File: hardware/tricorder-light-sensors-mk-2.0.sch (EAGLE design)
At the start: 8 parts, among them U1 VEML6075, U2 APDS-9250

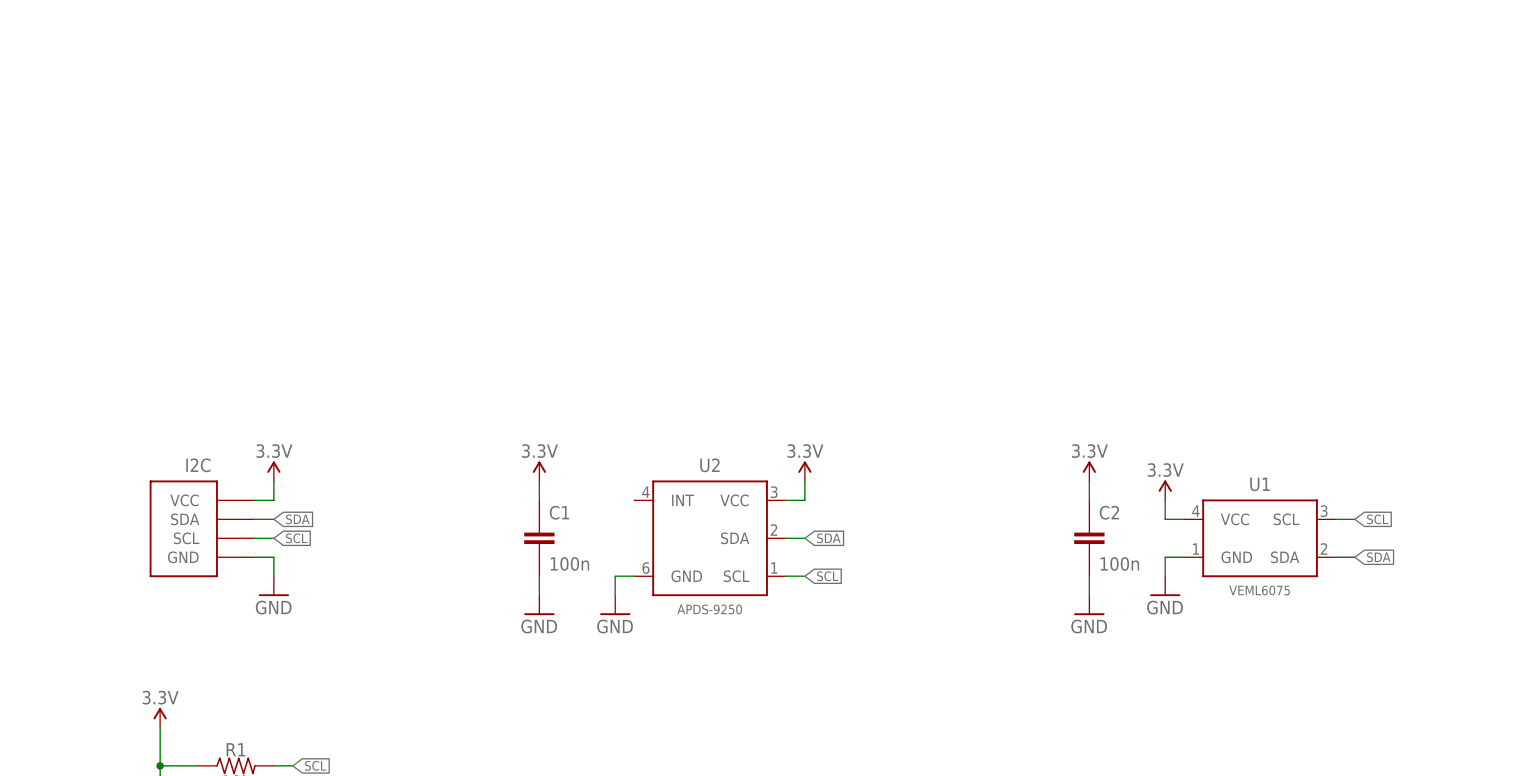
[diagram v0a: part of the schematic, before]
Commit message: swap apds9250 for tcs3400
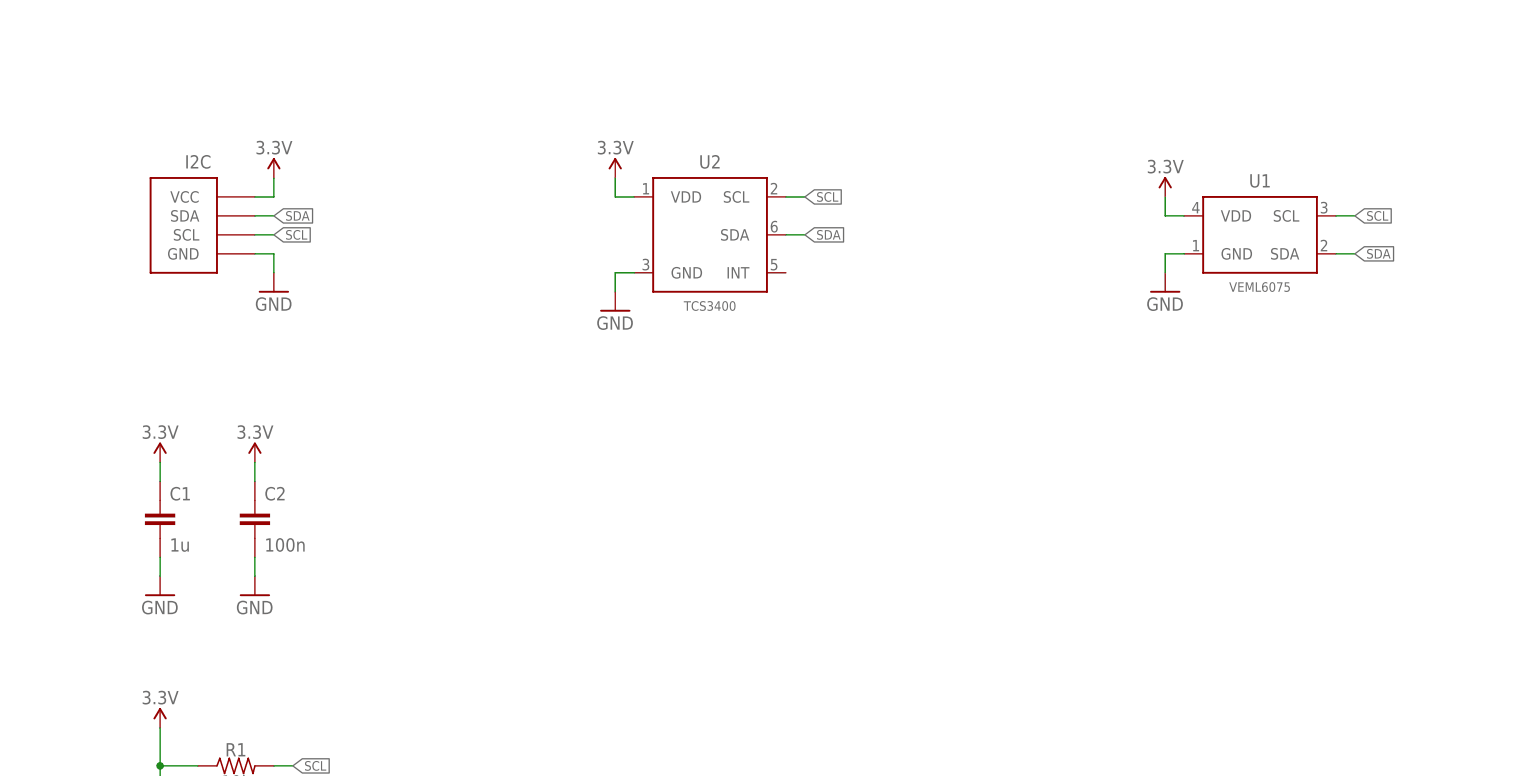
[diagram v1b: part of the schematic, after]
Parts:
- C1: value 100n -> 1u
- U2: value APDS-9250 -> TCS3400; device a_parts:APDS-9250ALT -> a_parts:TCS3400DFN6
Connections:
- net 3.3V: now also U1.VDD, U2.VDD; no longer U1.VCC, U2.VCC
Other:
- moved on the sheet: C1, C2, I2C, U1, U2
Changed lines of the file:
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@@
 </part>
 <part name="GND1" library="a_parts" deviceset="GND" device=""/>
-<part name="C1" library="a_parts" deviceset="CAPACITOR-CERAMIC" device="C0603" value="100n"/>
+<part name="C1" library="a_parts" deviceset="CAPACITOR-CERAMIC" device="C0603" value="1u"/>
 <part name="SUPPLY3" library="a_parts" deviceset="3.3V" device=""/>
 <part name="C2" library="a_parts" deviceset="CAPACITOR-CERAMIC" device="C0603" value="100n"/>
 <part name="SUPPLY4" library="a_parts" deviceset="3.3V" device=""/>
 <part name="GND4" library="a_parts" deviceset="GND" device=""/>
-<part name="U2" library="a_parts" deviceset="APDS-9250" device="ALT" value="APDS-9250"/>
 <part name="U1" library="a_parts" deviceset="VEML6075" device=""/>
 <part name="I2C" library="a_parts" deviceset="M04-I2C" device="PTH-0.1IN-CENTERED" value="M04-I2CPTH-0.1IN-CENTERED"/>
@@
 <part name="R1" library="a_parts" deviceset="RESISTOR" device="R0603" value="10k"/>
 <part name="R2" library="a_parts" deviceset="RESISTOR" device="R0603" value="10k"/>
+<part name="U2" library="a_parts" deviceset="TCS3400" device="DFN6" value="TCS3400"/>
 </parts>
 <sheets>
 <sheet>
 <plain>
-<text x="93.98" y="83.82" size="1.778" layer="90">RGB, IR, Ambient</text>
-<text x="172.72" y="83.82" size="1.778" layer="90">UVA, UVB</text>
+<text x="93.98" y="124.46" size="1.778" layer="90">RGB, IR, Ambient</text>
+<text x="172.72" y="124.46" size="1.778" layer="90">UVA, UVB</text>
 <wire x1="35.56" y1="185.42" x2="33.02" y2="185.42" width="0.1524" layer="90" style="shortdash"/>
 </plain>
@@
 <instance part="FRAME1" gate="G$1" x="0" y="0"/>
 <instance part="FRAME1" gate="V" x="152.4" y="0"/>
-<instance part="GND1" gate="1" x="81.28" y="91.44"/>
-<instance part="C1" gate="G$1" x="81.28" y="101.6"/>
-<instance part="SUPPLY3" gate="G$1" x="81.28" y="109.22"/>
-<instance part="C2" gate="G$1" x="154.94" y="101.6"/>
-<instance part="SUPPLY4" gate="G$1" x="154.94" y="109.22"/>
-<instance part="GND4" gate="1" x="154.94" y="91.44"/>
-<instance part="U2" gate="G$1" x="104.14" y="101.6"/>
-<instance part="U1" gate="G$1" x="177.8" y="101.6"/>
-<instance part="I2C" gate="G$1" x="35.56" y="104.14" rot="MR0"/>
-<instance part="SUPPLY1" gate="G$1" x="45.72" y="109.22"/>
-<instance part="GND2" gate="1" x="45.72" y="93.98"/>
-<instance part="SUPPLY2" gate="G$1" x="116.84" y="109.22"/>
-<instance part="SUPPLY5" gate="G$1" x="165.1" y="106.68"/>
-<instance part="GND7" gate="1" x="165.1" y="93.98"/>
-<instance part="GND8" gate="1" x="91.44" y="91.44"/>
+<instance part="GND1" gate="1" x="30.48" y="93.98"/>
+<instance part="C1" gate="G$1" x="30.48" y="104.14"/>
+<instance part="SUPPLY3" gate="G$1" x="30.48" y="111.76"/>
+<instance part="C2" gate="G$1" x="43.18" y="104.14"/>
+<instance part="SUPPLY4" gate="G$1" x="43.18" y="111.76"/>
+<instance part="GND4" gate="1" x="43.18" y="93.98"/>
+<instance part="U1" gate="G$1" x="177.8" y="142.24"/>
+<instance part="I2C" gate="G$1" x="35.56" y="144.78" rot="MR0"/>
+<instance part="SUPPLY1" gate="G$1" x="45.72" y="149.86"/>
+<instance part="GND2" gate="1" x="45.72" y="134.62"/>
+<instance part="SUPPLY2" gate="G$1" x="91.44" y="149.86"/>
+<instance part="SUPPLY5" gate="G$1" x="165.1" y="147.32"/>
+<instance part="GND7" gate="1" x="165.1" y="134.62"/>
+<instance part="GND8" gate="1" x="91.44" y="132.08"/>
 <instance part="SUPPLY8" gate="G$1" x="30.48" y="76.2"/>
 <instance part="R1" gate="G$1" x="40.64" y="71.12"/>
 <instance part="R2" gate="G$1" x="40.64" y="63.5"/>
+<instance part="U2" gate="G$1" x="104.14" y="142.24"/>
 </instances>
 <busses>
@@
 <pinref part="GND1" gate="1" pin="GND"/>
 <pinref part="C1" gate="G$1" pin="2"/>
-<wire x1="81.28" y1="96.52" x2="81.28" y2="93.98" width="0.1524" layer="91"/>
+<wire x1="30.48" y1="99.06" x2="30.48" y2="96.52" width="0.1524" layer="91"/>
 </segment>
 <segment>
 <pinref part="C2" gate="G$1" pin="2"/>
 <pinref part="GND4" gate="1" pin="GND"/>
-<wire x1="154.94" y1="93.98" x2="154.94" y2="96.52" width="0.1524" layer="91"/>
+<wire x1="43.18" y1="96.52" x2="43.18" y2="99.06" width="0.1524" layer="91"/>
 </segment>
 <segment>
 <pinref part="GND2" gate="1" pin="GND"/>
-<wire x1="45.72" y1="96.52" x2="45.72" y2="99.06" width="0.1524" layer="91"/>
+<wire x1="45.72" y1="137.16" x2="45.72" y2="139.7" width="0.1524" layer="91"/>
 <pinref part="I2C" gate="G$1" pin="GND"/>
-<wire x1="45.72" y1="99.06" x2="43.18" y2="99.06" width="0.1524" layer="91"/>
+<wire x1="45.72" y1="139.7" x2="43.18" y2="139.7" width="0.1524" layer="91"/>
 </segment>
 <segment>
 <pinref part="GND7" gate="1" pin="GND"/>
-<wire x1="165.1" y1="96.52" x2="165.1" y2="99.06" width="0.1524" layer="91"/>
+<wire x1="165.1" y1="137.16" x2="165.1" y2="139.7" width="0.1524" layer="91"/>
 <pinref part="U1" gate="G$1" pin="GND"/>
-<wire x1="165.1" y1="99.06" x2="167.64" y2="99.06" width="0.1524" layer="91"/>
+<wire x1="165.1" y1="139.7" x2="167.64" y2="139.7" width="0.1524" layer="91"/>
 </segment>
 <segment>
-<wire x1="91.44" y1="93.98" x2="91.44" y2="96.52" width="0.1524" layer="91"/>
+<wire x1="91.44" y1="134.62" x2="91.44" y2="137.16" width="0.1524" layer="91"/>
+<wire x1="91.44" y1="137.16" x2="93.98" y2="137.16" width="0.1524" layer="91"/>
+<pinref part="GND8" gate="1" pin="GND"/>
 <pinref part="U2" gate="G$1" pin="GND"/>
-<wire x1="91.44" y1="96.52" x2="93.98" y2="96.52" width="0.1524" layer="91"/>
-<pinref part="GND8" gate="1" pin="GND"/>
 </segment>
 </net>
@@
 <pinref part="C1" gate="G$1" pin="1"/>
 <pinref part="SUPPLY3" gate="G$1" pin="3.3V"/>
-<wire x1="81.28" y1="109.22" x2="81.28" y2="106.68" width="0.1524" layer="91"/>
+<wire x1="30.48" y1="111.76" x2="30.48" y2="109.22" width="0.1524" layer="91"/>
 </segment>
 <segment>
 <pinref part="C2" gate="G$1" pin="1"/>
 <pinref part="SUPPLY4" gate="G$1" pin="3.3V"/>
-<wire x1="154.94" y1="109.22" x2="154.94" y2="106.68" width="0.1524" layer="91"/>
+<wire x1="43.18" y1="111.76" x2="43.18" y2="109.22" width="0.1524" layer="91"/>
 </segment>
 <segment>
 <pinref part="SUPPLY1" gate="G$1" pin="3.3V"/>
-<wire x1="45.72" y1="109.22" x2="45.72" y2="106.68" width="0.1524" layer="91"/>
+<wire x1="45.72" y1="149.86" x2="45.72" y2="147.32" width="0.1524" layer="91"/>
 <pinref part="I2C" gate="G$1" pin="VCC"/>
-<wire x1="45.72" y1="106.68" x2="43.18" y2="106.68" width="0.1524" layer="91"/>
+<wire x1="45.72" y1="147.32" x2="43.18" y2="147.32" width="0.1524" layer="91"/>
 </segment>
 <segment>
-<pinref part="U2" gate="G$1" pin="VCC"/>
-<wire x1="114.3" y1="106.68" x2="116.84" y2="106.68" width="0.1524" layer="91"/>
+<wire x1="93.98" y1="147.32" x2="91.44" y2="147.32" width="0.1524" layer="91"/>
 <pinref part="SUPPLY2" gate="G$1" pin="3.3V"/>
-<wire x1="116.84" y1="106.68" x2="116.84" y2="109.22" width="0.1524" layer="91"/>
+<wire x1="91.44" y1="147.32" x2="91.44" y2="149.86" width="0.1524" layer="91"/>
+<pinref part="U2" gate="G$1" pin="VDD"/>
 </segment>
 <segment>
 <pinref part="SUPPLY5" gate="G$1" pin="3.3V"/>
-<wire x1="165.1" y1="106.68" x2="165.1" y2="104.14" width="0.1524" layer="91"/>
-<pinref part="U1" gate="G$1" pin="VCC"/>
-<wire x1="165.1" y1="104.14" x2="167.64" y2="104.14" width="0.1524" layer="91"/>
+<wire x1="165.1" y1="147.32" x2="165.1" y2="144.78" width="0.1524" layer="91"/>
+<pinref part="U1" gate="G$1" pin="VDD"/>
+<wire x1="165.1" y1="144.78" x2="167.64" y2="144.78" width="0.1524" layer="91"/>
 </segment>
 <segment>
@@
 <segment>
 <pinref part="I2C" gate="G$1" pin="SDA"/>
-<wire x1="45.72" y1="104.14" x2="43.18" y2="104.14" width="0.1524" layer="91"/>
-<label x="45.72" y="104.14" size="1.27" layer="95" xref="yes"/>
+<wire x1="45.72" y1="144.78" x2="43.18" y2="144.78" width="0.1524" layer="91"/>
+<label x="45.72" y="144.78" size="1.27" layer="95" xref="yes"/>
 </segment>
 <segment>
-<wire x1="116.84" y1="101.6" x2="114.3" y2="101.6" width="0.1524" layer="91"/>
-<label x="116.84" y="101.6" size="1.27" layer="95" xref="yes"/>
+<wire x1="116.84" y1="142.24" x2="114.3" y2="142.24" width="0.1524" layer="91"/>
+<label x="116.84" y="142.24" size="1.27" layer="95" xref="yes"/>
 <pinref part="U2" gate="G$1" pin="SDA"/>
 </segment>
 <segment>
-<wire x1="190.5" y1="99.06" x2="187.96" y2="99.06" width="0.1524" layer="91"/>
-<label x="190.5" y="99.06" size="1.27" layer="95" xref="yes"/>
+<wire x1="190.5" y1="139.7" x2="187.96" y2="139.7" width="0.1524" layer="91"/>
+<label x="190.5" y="139.7" size="1.27" layer="95" xref="yes"/>
 <pinref part="U1" gate="G$1" pin="SDA"/>
 </segment>
@@
 <segment>
 <pinref part="I2C" gate="G$1" pin="SCL"/>
-<wire x1="45.72" y1="101.6" x2="43.18" y2="101.6" width="0.1524" layer="91"/>
-<label x="45.72" y="101.6" size="1.27" layer="95" xref="yes"/>
+<wire x1="45.72" y1="142.24" x2="43.18" y2="142.24" width="0.1524" layer="91"/>
+<label x="45.72" y="142.24" size="1.27" layer="95" xref="yes"/>
 </segment>
 <segment>
-<wire x1="116.84" y1="96.52" x2="114.3" y2="96.52" width="0.1524" layer="91"/>
-<label x="116.84" y="96.52" size="1.27" layer="95" xref="yes"/>
+<wire x1="116.84" y1="147.32" x2="114.3" y2="147.32" width="0.1524" layer="91"/>
+<label x="116.84" y="147.32" size="1.27" layer="95" xref="yes"/>
 <pinref part="U2" gate="G$1" pin="SCL"/>
 </segment>
 <segment>
-<wire x1="190.5" y1="104.14" x2="187.96" y2="104.14" width="0.1524" layer="91"/>
-<label x="190.5" y="104.14" size="1.27" layer="95" xref="yes"/>
+<wire x1="190.5" y1="144.78" x2="187.96" y2="144.78" width="0.1524" layer="91"/>
+<label x="190.5" y="144.78" size="1.27" layer="95" xref="yes"/>
 <pinref part="U1" gate="G$1" pin="SCL"/>
 </segment>
